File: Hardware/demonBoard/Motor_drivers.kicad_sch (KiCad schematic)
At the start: 20 parts, among them J10 MOTOR_RIGHT_CONN, J3 LED_LEFT_CONN, J4 LED_TAIL_CONN, J5 LED_RIGHT_CONN, J6 BATT_CONN, J7 LED_AUX1_CONN, J8 LED_AUX2_CONN, J9 MOTOR_LEFT_CONN, U4 DRV8871DDA, U5 DRV8871DDA

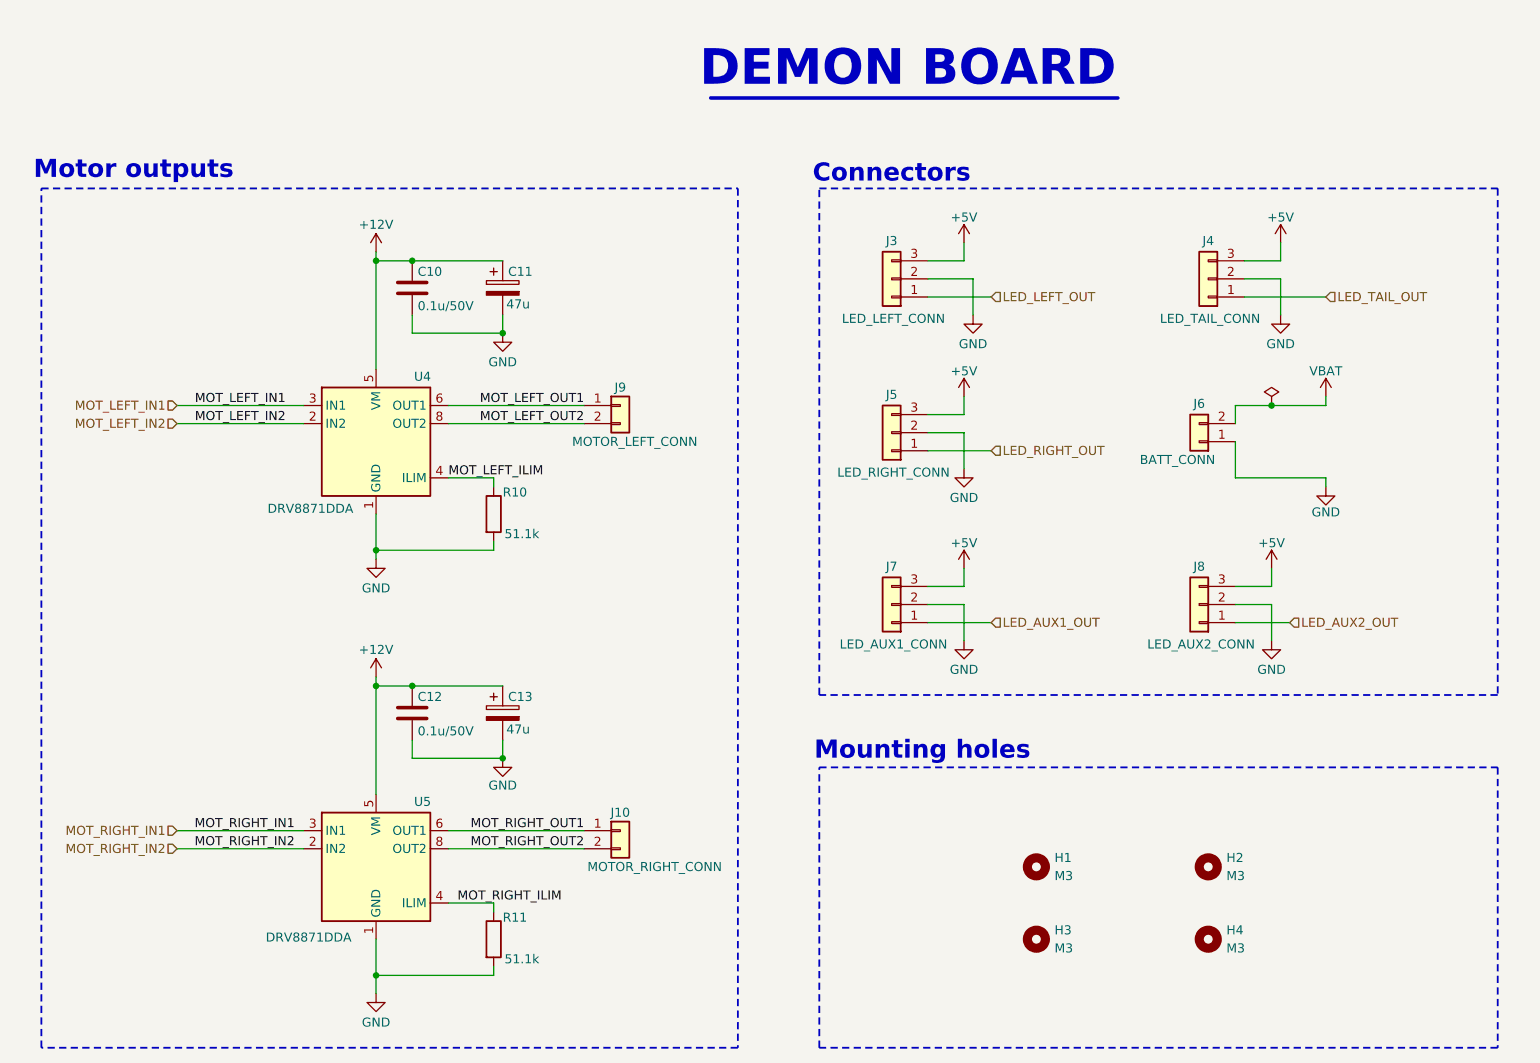
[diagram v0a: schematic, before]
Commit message: doc: Add schematic pdf
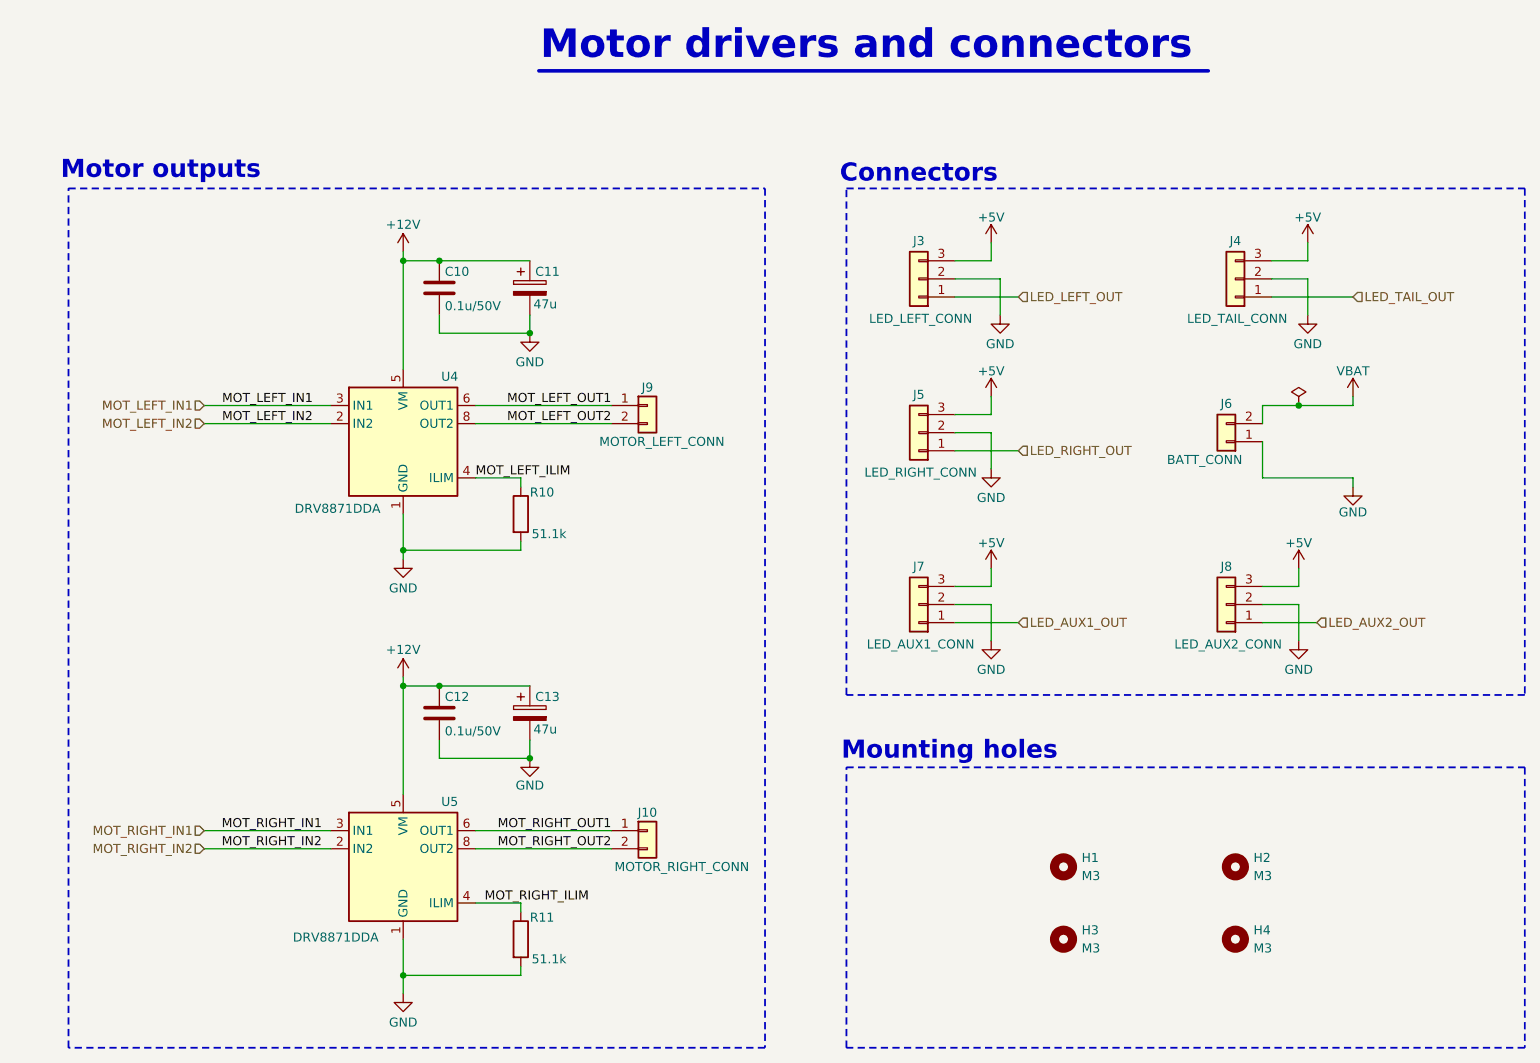
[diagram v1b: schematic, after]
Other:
- note added: "Motor drivers and connectors"
- note removed: "DEMON BOARD"
- company: (none) -> Vagarth Gaurav
- title: (none) -> Demon board
- moved on the sheet: C10, C11, C12, C13, H1, H2, H3, H4, J10, J3, J4, J5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
